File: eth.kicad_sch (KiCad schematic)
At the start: 58 parts, among them U501 KSZ9131RNXC, Y502 Resonator_25MHz_ECX-1247Q

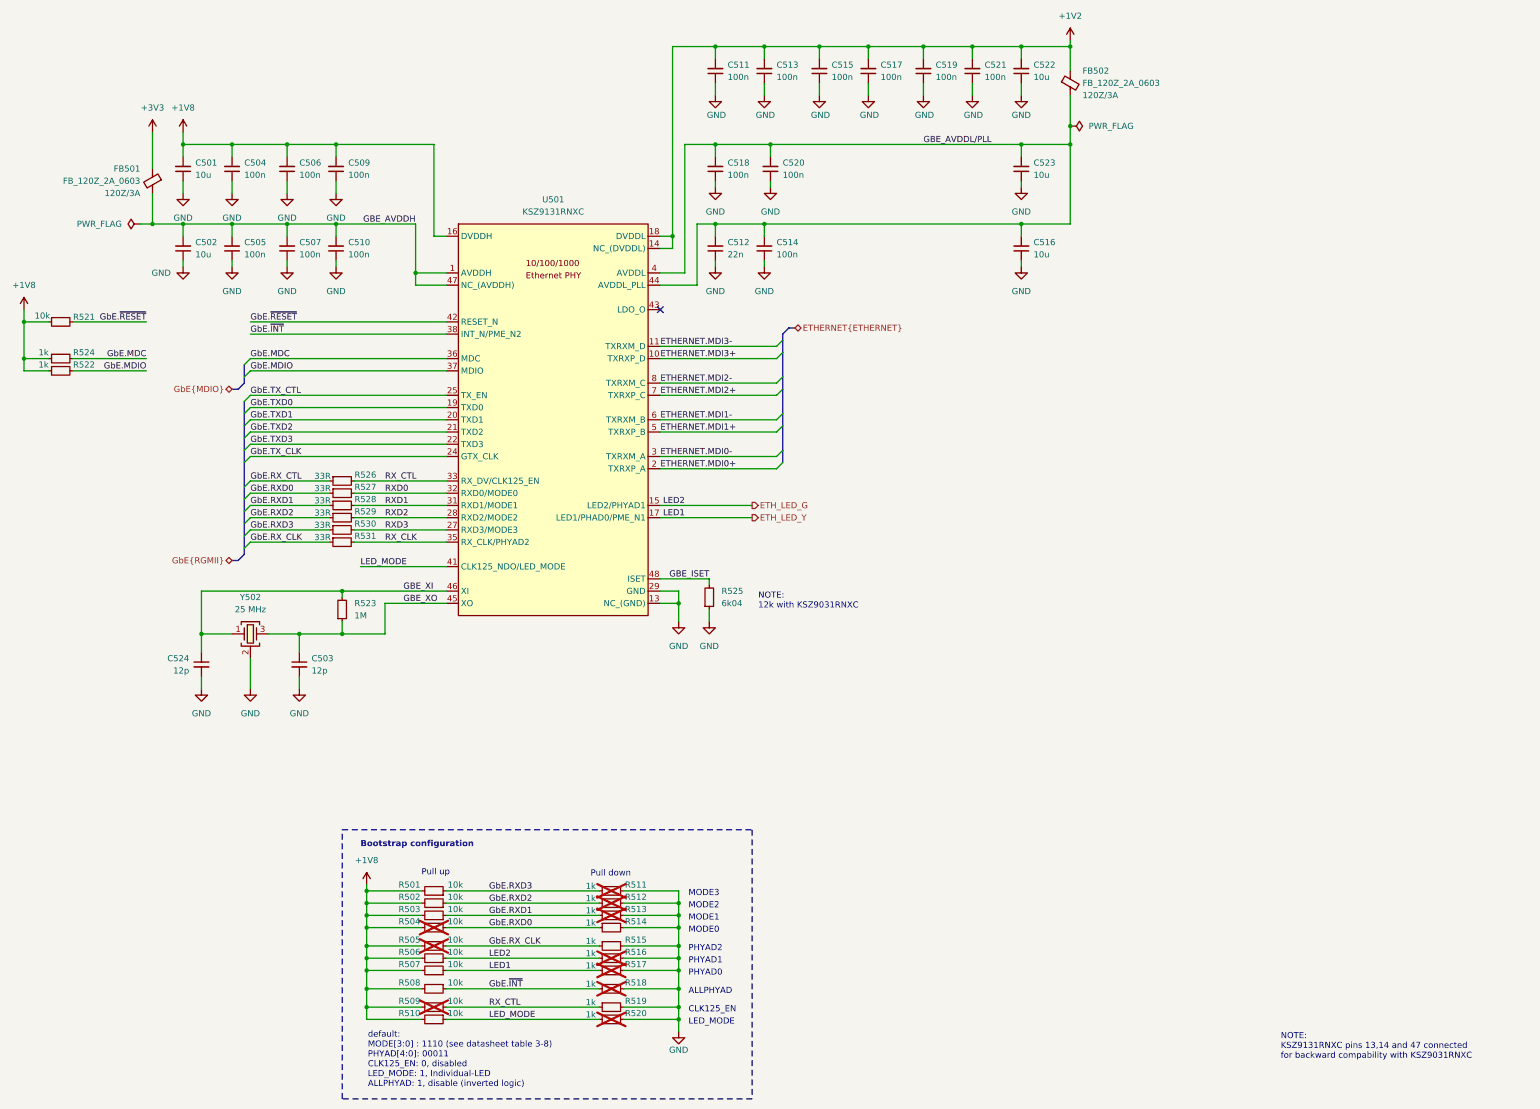
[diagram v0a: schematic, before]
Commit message: [#100282] Reorder schematic pages, reannotate schematic
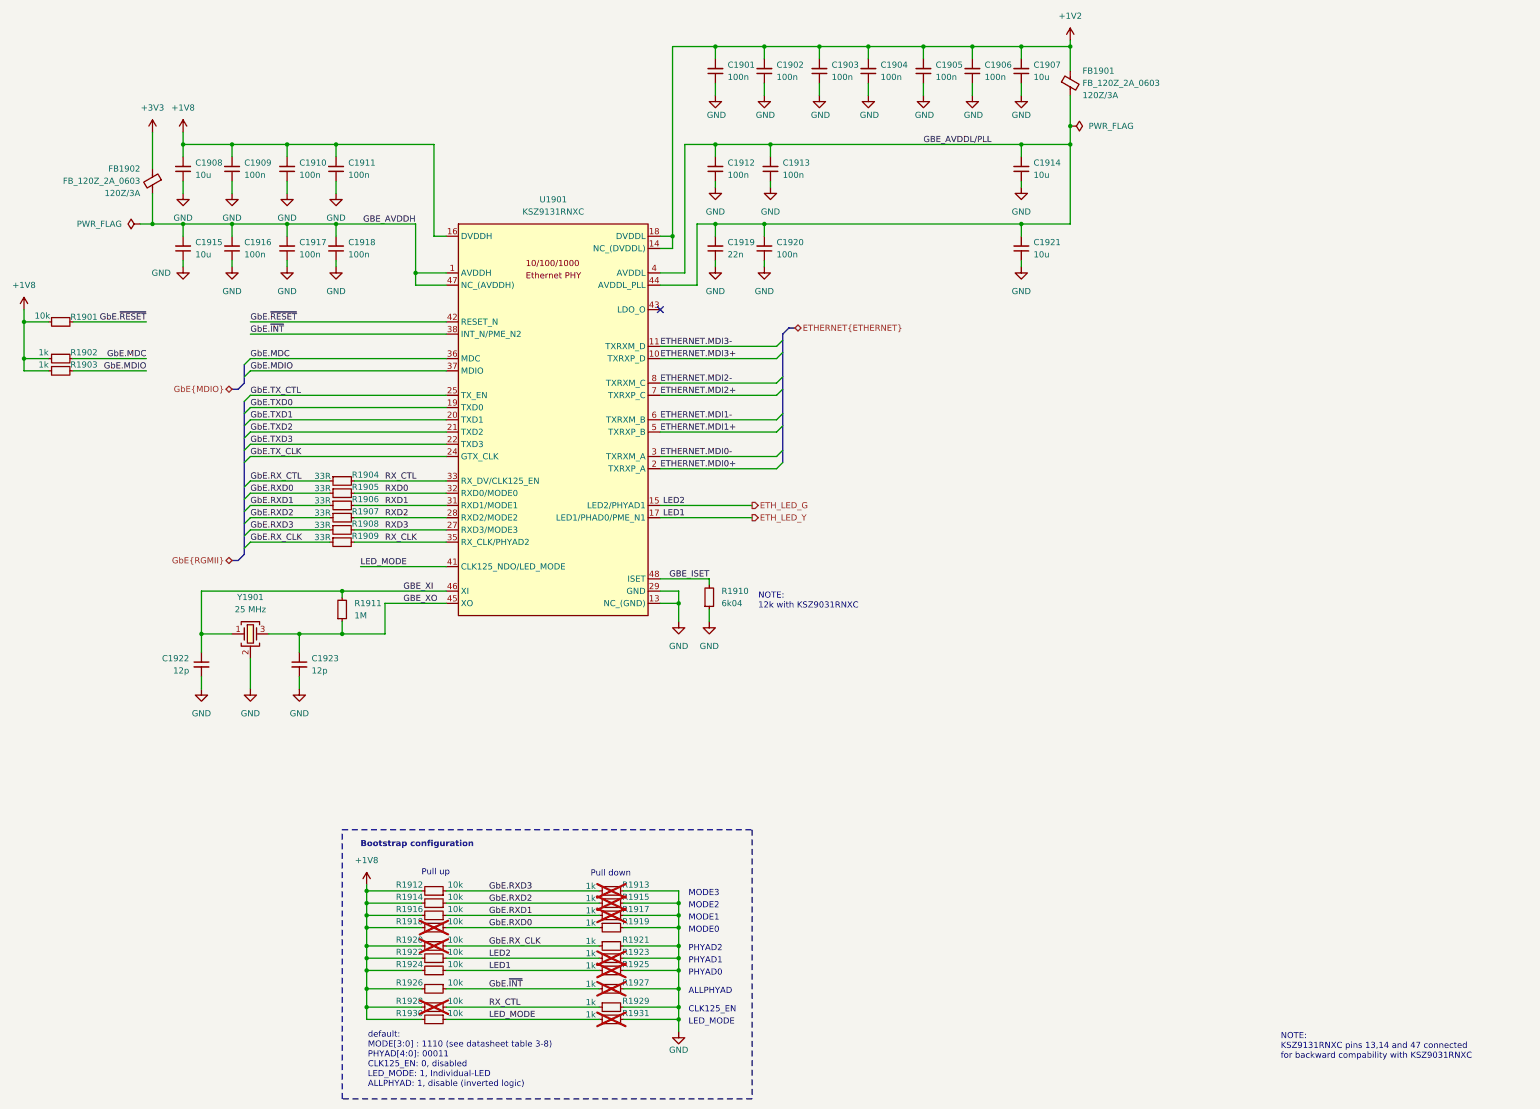
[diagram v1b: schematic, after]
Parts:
- renumbered C511 to C1901, C513 to C1902, C515 to C1903, C517 to C1904, C519 to C1905, C521 to C1906, C522 to C1907, C501 to C1908, C504 to C1909, C506 to C1910, C509 to C1911, C518 to C1912, C520 to C1913, C523 to C1914, C502 to C1915, C505 to C1916, C507 to C1917, C510 to C1918, C512 to C1919, C514 to C1920, C516 to C1921, C524 to C1922, C503 to C1923, FB502 to FB1901, FB501 to FB1902, R521 to R1901, R524 to R1902, R522 to R1903, R526 to R1904, R527 to R1905, R528 to R1906, R529 to R1907, R530 to R1908, R531 to R1909, R525 to R1910, R523 to R1911, R501 to R1912, R511 to R1913, R502 to R1914, R512 to R1915, R503 to R1916, R513 to R1917, R504 to R1918, R514 to R1919, R505 to R1920, R515 to R1921, R506 to R1922, R516 to R1923, R507 to R1924, R517 to R1925, R508 to R1926, R518 to R1927, R509 to R1928, R519 to R1929, R510 to R1930, R520 to R1931, U501 to U1901, Y502 to Y1901

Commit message: [#100282] Update components from library
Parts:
- C1907, C1908, C1914, C1915, C1921: Manufacturer Yaego -> YAGEO
- U1901: Manufacturer Microchip -> Microchip Technology
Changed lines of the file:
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@@
 			)
 		)
-		(property "Description" ""
+		(property "Description" "SMD Chip Resistor, 10 kohm, ± 1%, 62.5 mW, 0402 [1005 Metric], Thick Film, General Purpose"
 			(at 189.23 236.22 0)
+			(hide yes)
 			(show_name no)
 			(do_not_autoplace no)
@@
 			)
 		)
-		(property "DNP" ""
-			(at 223.52 215.9 0)
-			(show_name no)
-			(do_not_autoplace no)
-			(effects
-				(font
-					(size 1.27 1.27)
-				)
-			)
-		)
 		(property "License" "Apache-2.0"
 			(at 241.3 241.3 0)
@@
 			)
 		)
-		(property "Datasheet" ""
+		(property "Datasheet" "https://www.yageo.com/en/Chart/Download/pdf/CC0402MRX5R5BB106"
 			(at 323.85 64.77 0)
 			(hide yes)
@@
 			)
 		)
-		(property "Description" ""
+		(property "Description" "SMD Multilayer Ceramic Capacitor, 10 µF, 6.3 V, 0402 [1005 Metric], ± 20%, X5R, CC Series"
 			(at 308.61 85.09 0)
+			(hide yes)
 			(show_name no)
 			(do_not_autoplace no)
@@
 			)
 		)
-		(property "Manufacturer" "Yaego"
+		(property "Manufacturer" "YAGEO"
 			(at 328.93 64.77 0)
 			(hide yes)
@@
 			)
 		)
-		(property "Description" ""
+		(property "Description" "SMD Chip Resistor, 1 Mohm, ± 1%, 62.5 mW, 0402 [1005 Metric], Thick Film, General Purpose"
 			(at 167.64 160.02 0)
+			(hide yes)
 			(show_name no)
 			(do_not_autoplace no)
@@
 		(property "Description" ""
 			(at 318.77 57.15 0)
+			(hide yes)
 			(show_name no)
 			(do_not_autoplace no)
@@
 			)
 		)
-		(property "DNP" ""
-			(at 223.52 229.87 0)
-			(show_name no)
-			(do_not_autoplace no)
-			(effects
-				(font
-					(size 1.27 1.27)
-				)
-			)
-		)
 		(property "License" "Apache-2.0"
 			(at 241.3 255.27 0)
@@
 			)
 		)
-		(property "Description" ""
+		(property "Description" "SMD Chip Resistor, 10 kohm, ± 1%, 62.5 mW, 0402 [1005 Metric], Thick Film, General Purpose"
 			(at 189.23 227.33 0)
+			(hide yes)
 			(show_name no)
 			(do_not_autoplace no)
@@
 			)
 		)
-		(property "DNP" ""
-			(at 186.69 227.33 0)
-			(show_name no)
-			(do_not_autoplace no)
-			(effects
-				(font
-					(size 1.27 1.27)
-				)
-			)
-		)
 		(property "License" "Apache-2.0"
 			(at 168.91 201.93 0)
@@
 			)
 		)
-		(property "Datasheet" ""
+		(property "Datasheet" "https://www.yageo.com/en/Chart/Download/pdf/CC0402MRX5R5BB106"
 			(at 323.85 27.94 0)
 			(hide yes)
@@
 			)
 		)
-		(property "Description" ""
+		(property "Description" "SMD Multilayer Ceramic Capacitor, 10 µF, 6.3 V, 0402 [1005 Metric], ± 20%, X5R, CC Series"
 			(at 308.61 48.26 0)
+			(hide yes)
 			(show_name no)
 			(do_not_autoplace no)
@@
 			)
 		)
-		(property "Manufacturer" "Yaego"
+		(property "Manufacturer" "YAGEO"
 			(at 328.93 27.94 0)
 			(hide yes)
@@
 			)
 		)
-		(property "Description" ""
+		(property "Description" "SMD Chip Resistor, 1 kohm, ± 1%, 63 mW, 0402 [1005 Metric], Thick Film, General Purpose"
 			(at 106.68 107.95 0)
+			(hide yes)
 			(show_name no)
 			(do_not_autoplace no)
@@
 		(property "Description" ""
 			(at 125.73 77.47 0)
+			(hide yes)
 			(show_name no)
 			(do_not_autoplace no)
@@
 			)
 		)
-		(property "Description" ""
+		(property "Description" "SMD Chip Resistor, 10 kohm, ± 1%, 62.5 mW, 0402 [1005 Metric], Thick Film, General Purpose"
 			(at 189.23 240.03 0)
+			(hide yes)
 			(show_name no)
 			(do_not_autoplace no)
@@
 			)
 		)
-		(property "DNP" ""
-			(at 186.69 240.03 0)
-			(show_name no)
-			(do_not_autoplace no)
-			(effects
-				(font
-					(size 1.27 1.27)
-				)
-			)
-		)
 		(property "License" "Apache-2.0"
 			(at 168.91 265.43 0)
@@
 			)
 		)
-		(property "Description" ""
+		(property "Description" "SMD Chip Resistor, 10 kohm, ± 1%, 62.5 mW, 0402 [1005 Metric], Thick Film, General Purpose"
 			(at 189.23 218.44 0)
+			(hide yes)
 			(show_name no)
 			(do_not_autoplace no)
@@
 		(property "Tolerance" "0.1%"
 			(at 246.38 157.4799 90)
-			(hide yes)
 			(show_name no)
 			(do_not_autoplace no)
@@
 			)
 		)
-		(property "DNP" ""
-			(at 223.52 242.57 0)
-			(show_name no)
-			(do_not_autoplace no)
-			(effects
-				(font
-					(size 1.27 1.27)
-				)
-			)
-		)
 		(property "License" "Apache-2.0"
 			(at 241.3 267.97 0)
@@
 			)
 		)
-		(property "Datasheet" ""
+		(property "Datasheet" "https://www.yageo.com/en/Chart/Download/pdf/CC0402MRX5R5BB106"
 			(at 323.85 48.26 0)
 			(hide yes)
@@
 			)
 		)
-		(property "Description" ""
+		(property "Description" "SMD Multilayer Ceramic Capacitor, 10 µF, 6.3 V, 0402 [1005 Metric], ± 20%, X5R, CC Series"
 			(at 308.61 68.58 0)
+			(hide yes)
 			(show_name no)
 			(do_not_autoplace no)
@@
 			)
 		)
-		(property "Manufacturer" "Yaego"
+		(property "Manufacturer" "YAGEO"
 			(at 328.93 48.26 0)
 			(hide yes)
@@
 			)
 		)
-		(property "Description" ""
+		(property "Description" "SMD Chip Resistor, 10 kohm, ± 1%, 62.5 mW, 0402 [1005 Metric], Thick Film, General Purpose"
 			(at 189.23 242.57 0)
+			(hide yes)
 			(show_name no)
 			(do_not_autoplace no)
@@
 			)
 		)
-		(property "Datasheet" ""
+		(property "Datasheet" "https://www.yageo.com/en/Chart/Download/pdf/CC0402MRX5R5BB106"
 			(at 149.86 48.26 0)
 			(hide yes)
@@
 			)
 		)
-		(property "Description" ""
+		(property "Description" "SMD Multilayer Ceramic Capacitor, 10 µF, 6.3 V, 0402 [1005 Metric], ± 20%, X5R, CC Series"
 			(at 134.62 68.58 0)
+			(hide yes)
 			(show_name no)
 			(do_not_autoplace no)
@@
 			)
 		)
-		(property "Manufacturer" "Yaego"
+		(property "Manufacturer" "YAGEO"
 			(at 154.94 48.26 0)
 			(hide yes)
@@
 			)
 		)
-		(property "Description" ""
+		(property "Description" "SMD Chip Resistor, 1 kohm, ± 1%, 63 mW, 0402 [1005 Metric], Thick Film, General Purpose"
 			(at 106.68 105.41 0)
+			(hide yes)
 			(show_name no)
 			(do_not_autoplace no)
@@
 			)
 		)
-		(property "Description" ""
+		(property "Description" "SMD Chip Resistor, 10 kohm, ± 1%, 62.5 mW, 0402 [1005 Metric], Thick Film, General Purpose"
 			(at 189.23 220.98 0)
+			(hide yes)
 			(show_name no)
 			(do_not_autoplace no)
@@
 			)
 		)
-		(property "DNP" ""
-			(at 186.69 220.98 0)
-			(show_name no)
-			(do_not_autoplace no)
-			(effects
-				(font
-					(size 1.27 1.27)
-				)
-			)
-		)
 		(property "License" "Apache-2.0"
 			(at 168.91 195.58 0)
@@
 			)
 		)
-		(property "Datasheet" ""
+		(property "Datasheet" "https://www.yageo.com/en/Chart/Download/pdf/CC0402MRX5R5BB106"
 			(at 149.86 64.77 0)
 			(hide yes)
@@
 			)
 		)
-		(property "Description" ""
+		(property "Description" "SMD Multilayer Ceramic Capacitor, 10 µF, 6.3 V, 0402 [1005 Metric], ± 20%, X5R, CC Series"
 			(at 134.62 85.09 0)
+			(hide yes)
 			(show_name no)
 			(do_not_autoplace no)
@@
 			)
 		)
-		(property "Manufacturer" "Yaego"
+		(property "Manufacturer" "YAGEO"
 			(at 154.94 64.77 0)
 			(hide yes)
@@
 			)
 		)
-		(property "Description" ""
+		(property "Description" "SMD Chip Resistor, 10 kohm, ± 1%, 62.5 mW, 0402 [1005 Metric], Thick Film, General Purpose"
 			(at 189.23 223.52 0)
+			(hide yes)
 			(show_name no)
 			(do_not_autoplace no)
@@
 			)
 		)
-		(property "DNP" ""
-			(at 186.69 223.52 0)
-			(show_name no)
-			(do_not_autoplace no)
-			(effects
-				(font
-					(size 1.27 1.27)
-				)
-			)
-		)
 		(property "License" "Apache-2.0"
 			(at 168.91 198.12 0)
@@
 		(property "Description" ""
 			(at 318.77 39.37 0)
+			(hide yes)
 			(show_name no)
 			(do_not_autoplace no)
@@
 			)
 		)
-		(property "Description" ""
+		(property "Description" "SMD Chip Resistor, 10 kohm, ± 1%, 62.5 mW, 0402 [1005 Metric], Thick Film, General Purpose"
 			(at 189.23 215.9 0)
+			(hide yes)
 			(show_name no)
 			(do_not_autoplace no)
@@
 			)
 		)
-		(property "Datasheet" ""
+		(property "Datasheet" "https://www.murata.com/products/productdetail?partno=GCM155R71H223MA55%23"
 			(at 260.35 64.77 0)
 			(hide yes)
@@
 			)
 		)
-		(property "Description" ""
+		(property "Description" "SMD Multilayer Ceramic Capacitors, 0.022 µF, 50 V, 20%, 0402 [1005 Metric], X7R"
 			(at 245.11 85.09 0)
+			(hide yes)
 			(show_name no)
 			(do_not_autoplace no)
@@
 			)
 		)
-		(property "DNP" ""
-			(at 223.52 236.22 0)
-			(show_name no)
-			(do_not_autoplace no)
-			(effects
-				(font
-					(size 1.27 1.27)
-				)
-			)
-		)
 		(property "License" "Apache-2.0"
 			(at 241.3 261.62 0)
@@
 			)
 		)
-		(property "DNP" ""
-			(at 223.52 218.44 0)
-			(show_name no)
-			(do_not_autoplace no)
-			(effects
-				(font
-					(size 1.27 1.27)
-				)
-			)
-		)
 		(property "License" "Apache-2.0"
 			(at 241.3 243.84 0)
@@
 			)
 		)
-		(property "Description" ""
+		(property "Description" "SMD Chip Resistor, 10 kohm, ± 1%, 62.5 mW, 0402 [1005 Metric], Thick Film, General Purpose"
 			(at 106.68 97.79 0)
+			(hide yes)
 			(show_name no)
 			(do_not_autoplace no)
@@
 			)
 		)
-		(property "Description" ""
+		(property "Description" "SMD Chip Resistor, 10 kohm, ± 1%, 62.5 mW, 0402 [1005 Metric], Thick Film, General Purpose"
 			(at 189.23 229.87 0)
+			(hide yes)
 			(show_name no)
 			(do_not_autoplace no)
@@
 			)
 		)
-		(property "DNP" ""
-			(at 223.52 232.41 0)
-			(show_name no)
-			(do_not_autoplace no)
-			(effects
-				(font
-					(size 1.27 1.27)
-				)
-			)
-		)
 		(property "License" "Apache-2.0"
 			(at 241.3 257.81 0)
@@
 			)
 		)
-		(property "Description" ""
+		(property "Description" "Ethernet ICs Gigabit Ethernet Transceiver with RGMII support"
 			(at 189.23 80.01 0)
+			(hide yes)
 			(show_name no)
 			(do_not_autoplace no)
@@
 			)
 		)
-		(property "Manufacturer" "Microchip"
+		(property "Manufacturer" "Microchip Technology"
 			(at 247.65 92.71 0)
 			(hide yes)
@@
 		(property "MPN" "KSZ9131RNXC"
 			(at 247.65 95.25 0)
-			(hide yes)
 			(show_name no)
 			(do_not_autoplace no)
@@
 			)
 		)
-		(property "Description" ""
+		(property "Description" "SMD Chip Resistor, 10 kohm, ± 1%, 62.5 mW, 0402 [1005 Metric], Thick Film, General Purpose"
 			(at 189.23 232.41 0)
+			(hide yes)
 			(show_name no)
 			(do_not_autoplace no)

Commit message: [#100282] Update selected symbols
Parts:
- C1901, C1902, C1903, C1904, C1905, C1906, C1909, C1910, C1911, C1912, C1913, C1916, C1917, C1918, C1920: value C_100n_0402_EIA -> C_100n_0402
- FB1901, FB1902: value FB_120Z_2A_0603 -> FB_120Z_3A_Murata-BLM18SG_0603
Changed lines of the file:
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@@
 			)
 		)
-		(property "Value" "C_100n_0402_EIA"
+		(property "Value" "C_100n_0402"
 			(at 154.94 64.77 0)
 			(hide yes)
@@
 		(property "MPN" "ECS-250-10-47Q-CES-TR"
 			(at 148.59 154.94 0)
-			(hide yes)
 			(show_name no)
 			(do_not_autoplace no)
@@
 			)
 		)
-		(property "Value" "FB_120Z_2A_0603"
+		(property "Value" "FB_120Z_3A_Murata-BLM18SG_0603"
 			(at 125.73 68.5419 90)
+			(hide yes)
 			(show_name no)
 			(do_not_autoplace no)
@@
 			)
 		)
-		(property "Value" "C_100n_0402_EIA"
+		(property "Value" "C_100n_0402"
 			(at 265.43 64.77 0)
 			(hide yes)
@@
 			)
 		)
-		(property "Value" "FB_120Z_2A_0603"
+		(property "Value" "FB_120Z_3A_Murata-BLM18SG_0603"
 			(at 321.31 48.2219 90)
+			(hide yes)
 			(show_name no)
 			(do_not_autoplace no)
@@
 			)
 		)
-		(property "Value" "C_100n_0402_EIA"
+		(property "Value" "C_100n_0402"
 			(at 176.53 64.77 0)
 			(hide yes)
@@
 			)
 		)
-		(property "Value" "C_100n_0402_EIA"
+		(property "Value" "C_100n_0402"
 			(at 298.45 27.94 0)
 			(hide yes)
@@
 			)
 		)
-		(property "Value" "C_100n_0402_EIA"
+		(property "Value" "C_100n_0402"
 			(at 266.7 48.26 0)
 			(hide yes)
@@
 			)
 		)
-		(property "Value" "C_100n_0402_EIA"
+		(property "Value" "C_100n_0402"
 			(at 166.37 64.77 0)
 			(hide yes)
@@
 			)
 		)
-		(property "Value" "C_100n_0402_EIA"
+		(property "Value" "C_100n_0402"
 			(at 265.43 27.94 0)
 			(hide yes)
@@
 			)
 		)
-		(property "Value" "C_100n_0402_EIA"
+		(property "Value" "C_100n_0402"
 			(at 308.61 27.94 0)
 			(hide yes)
@@
 			)
 		)
-		(property "Value" "C_100n_0402_EIA"
+		(property "Value" "C_100n_0402"
 			(at 154.94 48.26 0)
 			(hide yes)
@@
 			)
 		)
-		(property "Value" "C_100n_0402_EIA"
+		(property "Value" "C_100n_0402"
 			(at 166.37 48.26 0)
 			(hide yes)
@@
 			)
 		)
-		(property "Value" "C_100n_0402_EIA"
+		(property "Value" "C_100n_0402"
 			(at 255.27 27.94 0)
 			(hide yes)
@@
 			)
 		)
-		(property "Value" "C_100n_0402_EIA"
+		(property "Value" "C_100n_0402"
 			(at 287.02 27.94 0)
 			(hide yes)
@@
 			)
 		)
-		(property "Value" "C_100n_0402_EIA"
+		(property "Value" "C_100n_0402"
 			(at 276.86 27.94 0)
 			(hide yes)
@@
 			)
 		)
-		(property "Value" "C_100n_0402_EIA"
+		(property "Value" "C_100n_0402"
 			(at 255.27 48.26 0)
 			(hide yes)
@@
 		(property "Value" "KSZ9131RNXC"
 			(at 211.455 74.93 0)
+			(hide yes)
 			(show_name no)
 			(do_not_autoplace no)
@@
 			)
 		)
-		(property "Value" "C_100n_0402_EIA"
+		(property "Value" "C_100n_0402"
 			(at 176.53 48.26 0)
 			(hide yes)
